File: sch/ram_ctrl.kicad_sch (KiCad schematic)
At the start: 11 parts

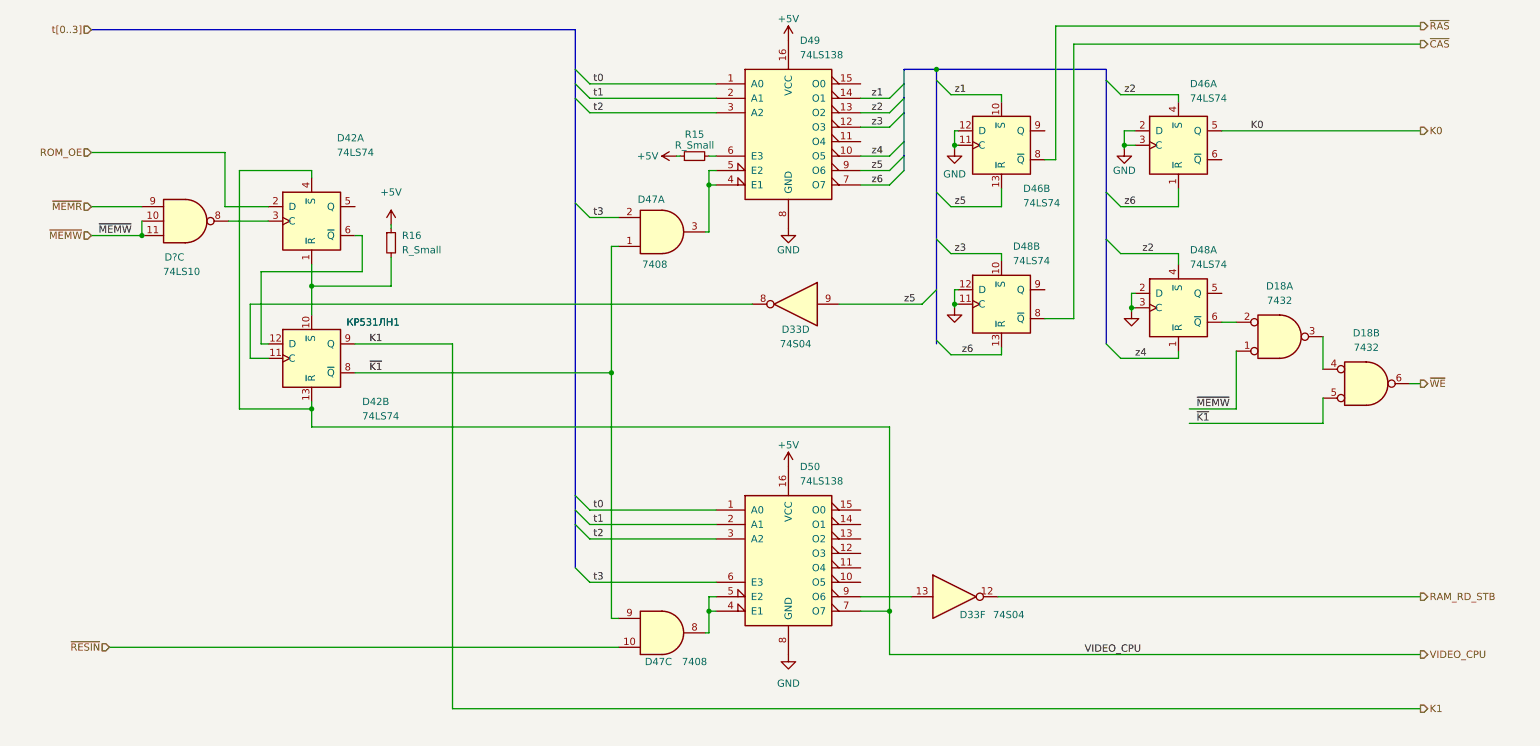
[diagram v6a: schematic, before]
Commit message: Schematics complete
Todo:
- part values
- full review
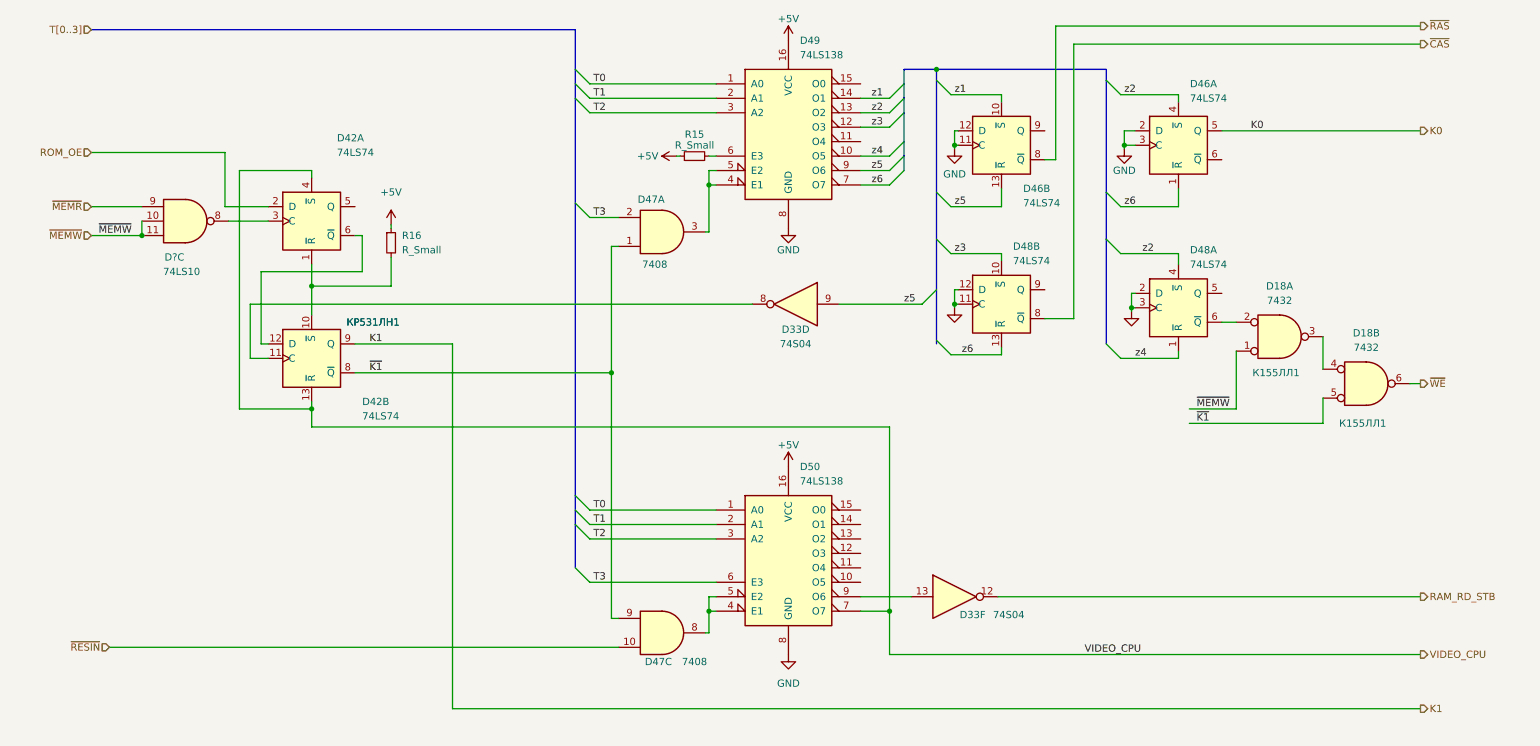
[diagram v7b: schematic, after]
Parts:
- D18: CCCP (none) -> К155ЛЛ1
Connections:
- net t0 renamed T0
- net t1 renamed T1
- net t2 renamed T2
- net t3 renamed T3
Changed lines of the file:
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@@
     (effects (font (size 1.27 1.27)) (justify left bottom))
   )
-  (label "t3" (at 119.38 124.46 0)
+  (label "T3" (at 119.38 124.46 0)
     (effects (font (size 1.27 1.27)) (justify left bottom))
   )
@@
     (effects (font (size 1.27 1.27)) (justify left bottom))
   )
-  (label "t0" (at 119.38 111.76 0)
+  (label "T0" (at 119.38 111.76 0)
     (effects (font (size 1.27 1.27)) (justify left bottom))
   )
@@
     (effects (font (size 1.27 1.27)) (justify left bottom))
   )
-  (label "t2" (at 119.38 116.84 0)
+  (label "T2" (at 119.38 116.84 0)
     (effects (font (size 1.27 1.27)) (justify left bottom))
   )
@@
     (effects (font (size 1.27 1.27)) (justify left bottom))
   )
-  (label "t1" (at 119.38 114.3 0)
+  (label "T1" (at 119.38 114.3 0)
     (effects (font (size 1.27 1.27)) (justify left bottom))
   )
@@
     (effects (font (size 1.27 1.27)) (justify left bottom))
   )
-  (label "t0" (at 119.38 36.83 0)
-    (effects (font (size 1.27 1.27)) (justify left bottom))
-  )
-  (label "t3" (at 119.38 60.325 0)
-    (effects (font (size 1.27 1.27)) (justify left bottom))
-  )
-  (label "t2" (at 119.38 41.91 0)
+  (label "T0" (at 119.38 36.83 0)
+    (effects (font (size 1.27 1.27)) (justify left bottom))
+  )
+  (label "T3" (at 119.38 60.325 0)
+    (effects (font (size 1.27 1.27)) (justify left bottom))
+  )
+  (label "T2" (at 119.38 41.91 0)
     (effects (font (size 1.27 1.27)) (justify left bottom))
   )
@@
     (effects (font (size 1.27 1.27)) (justify left bottom))
   )
-  (label "t1" (at 119.38 39.37 0)
+  (label "T1" (at 119.38 39.37 0)
     (effects (font (size 1.27 1.27)) (justify left bottom))
   )
@@
     (effects (font (size 1.27 1.27)) (justify right))
   )
-  (hierarchical_label "t[0..3]" (shape input) (at 31.115 27.305 180)
+  (hierarchical_label "T[0..3]" (shape input) (at 31.115 27.305 180)
     (effects (font (size 1.27 1.27)) (justify right))
   )
@@
   )
   (symbol (lib_id "74xx:74LS32") (at 255.27 89.535 0) (unit 2) (convert 2)
-    (in_bom yes) (on_board yes) (fields_autoplaced)
+    (in_bom yes) (on_board yes)
     (property "Reference" "D18" (id 0) (at 255.27 80.645 0))
     (property "Value" "7432" (id 1) (at 255.27 83.185 0))
@@
       (effects (font (size 1.27 1.27)) hide)
     )
+    (property "CCCP" "К155ЛЛ1" (id 4) (at 254.635 96.52 0))
     (pin "1")
     (pin "2")
@@
   )
   (symbol (lib_id "74xx:74LS32") (at 240.03 81.28 0) (mirror x) (unit 1) (convert 2)
-    (in_bom yes) (on_board yes) (fields_autoplaced)
+    (in_bom yes) (on_board yes)
     (property "Reference" "D18" (id 0) (at 240.03 72.39 0))
     (property "Value" "7432" (id 1) (at 240.03 74.93 0))
@@
       (effects (font (size 1.27 1.27)) hide)
     )
-    (pin "1")
-    (pin "2")
+    (property "CCCP" "К155ЛЛ1" (id 4) (at 239.395 87.63 0))
+    (pin "1")
+    (pin "2")

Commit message: Schematics completed with values
Visual corrections pending
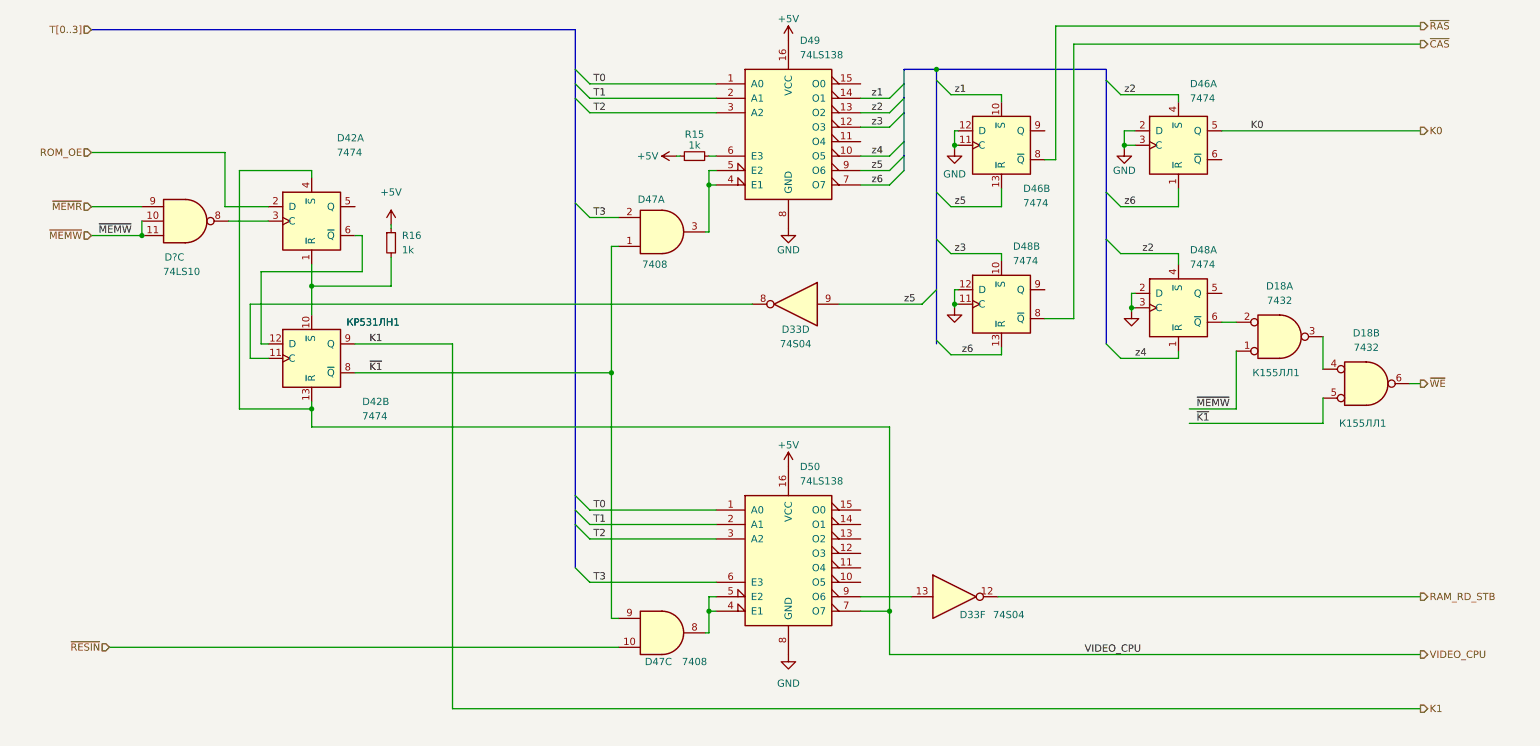
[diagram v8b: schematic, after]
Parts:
- D42, D46, D48: value 74LS74 -> 7474; CCCP (none) -> К155ТМ2
- D47: CCCP (none) -> К155ЛИ1
- D49, D50: CCCP (none) -> К155ИД7
- R15, R16: value R_Small -> 1k
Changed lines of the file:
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@@
       (effects (font (size 1.27 1.27)) (justify left))
     )
-    (property "Value" "74LS74" (id 1) (at 224.2694 39.37 0)
+    (property "Value" "7474" (id 1) (at 224.2694 39.37 0)
       (effects (font (size 1.27 1.27)) (justify left))
     )
@@
     )
     (property "Datasheet" "74xx/74hc_hct74.pdf" (id 3) (at 222.25 47.625 0)
+      (effects (font (size 1.27 1.27)) hide)
+    )
+    (property "CCCP" "К155ТМ2" (id 4) (at 222.25 47.625 0)
       (effects (font (size 1.27 1.27)) hide)
     )
@@
       (effects (font (size 1.27 1.27)) (justify left))
     )
-    (property "Value" "74LS74" (id 1) (at 78.74 95.25 0)
+    (property "Value" "7474" (id 1) (at 78.74 95.25 0)
       (effects (font (size 1.27 1.27)) (justify left))
     )
@@
     )
     (property "Datasheet" "74xx/74hc_hct74.pdf" (id 3) (at 69.85 85.09 0)
+      (effects (font (size 1.27 1.27)) hide)
+    )
+    (property "CCCP" "К155ТМ2" (id 4) (at 69.85 85.09 0)
       (effects (font (size 1.27 1.27)) hide)
     )
@@
       (effects (font (size 1.27 1.27)) hide)
     )
+    (property "CCCP" "К155ЛИ1" (id 4) (at 131.445 133.35 0)
+      (effects (font (size 1.27 1.27)) hide)
+    )
     (pin "1")
     (pin "2")
@@
       (effects (font (size 1.27 1.27)) (justify left))
     )
-    (property "Value" "74LS74" (id 1) (at 224.2694 68.58 0)
+    (property "Value" "7474" (id 1) (at 224.2694 68.58 0)
       (effects (font (size 1.27 1.27)) (justify left))
     )
@@
     )
     (property "Datasheet" "74xx/74hc_hct74.pdf" (id 3) (at 222.25 76.2 0)
+      (effects (font (size 1.27 1.27)) hide)
+    )
+    (property "CCCP" "К155ТМ2" (id 4) (at 222.25 76.2 0)
       (effects (font (size 1.27 1.27)) hide)
     )
@@
       (effects (font (size 1.27 1.27)) (justify left))
     )
-    (property "Value" "R_Small" (id 1) (at 85.725 66.0399 0)
+    (property "Value" "1k" (id 1) (at 85.725 66.0399 0)
       (effects (font (size 1.27 1.27)) (justify left))
     )
@@
       (effects (font (size 1.27 1.27)) hide)
     )
+    (property "CCCP" "К155ЛИ1" (id 4) (at 131.445 62.865 0)
+      (effects (font (size 1.27 1.27)) hide)
+    )
     (pin "1")
     (pin "2")
@@
       (effects (font (size 1.27 1.27)) (justify left))
     )
-    (property "Value" "74LS74" (id 1) (at 194.945 57.785 0)
+    (property "Value" "7474" (id 1) (at 194.945 57.785 0)
       (effects (font (size 1.27 1.27)) (justify left))
     )
@@
     )
     (property "Datasheet" "74xx/74hc_hct74.pdf" (id 3) (at 191.135 47.625 0)
+      (effects (font (size 1.27 1.27)) hide)
+    )
+    (property "CCCP" "К155ТМ2" (id 4) (at 191.135 47.625 0)
       (effects (font (size 1.27 1.27)) hide)
     )
@@
       (effects (font (size 1.27 1.27)) (justify left))
     )
-    (property "Value" "74LS74" (id 1) (at 74.295 48.895 0)
+    (property "Value" "7474" (id 1) (at 74.295 48.895 0)
       (effects (font (size 1.27 1.27)) (justify left))
     )
@@
     )
     (property "Datasheet" "74xx/74hc_hct74.pdf" (id 3) (at 69.85 60.96 0)
+      (effects (font (size 1.27 1.27)) hide)
+    )
+    (property "CCCP" "К155ТМ2" (id 4) (at 69.85 60.96 0)
       (effects (font (size 1.27 1.27)) hide)
     )
@@
       (effects (font (size 1.27 1.27)) (justify left))
     )
-    (property "Value" "74LS74" (id 1) (at 193.1544 67.945 0)
+    (property "Value" "7474" (id 1) (at 193.1544 67.945 0)
       (effects (font (size 1.27 1.27)) (justify left))
     )
@@
     )
     (property "Datasheet" "74xx/74hc_hct74.pdf" (id 3) (at 191.135 75.565 0)
+      (effects (font (size 1.27 1.27)) hide)
+    )
+    (property "CCCP" "К155ТМ2" (id 4) (at 191.135 75.565 0)
       (effects (font (size 1.27 1.27)) hide)
     )
@@
       (effects (font (size 1.27 1.27)) hide)
     )
+    (property "CCCP" "К155ИД7" (id 4) (at 153.67 119.38 0)
+      (effects (font (size 1.27 1.27)) hide)
+    )
     (pin "1")
     (pin "10")
@@
       (effects (font (size 1.27 1.27)) hide)
     )
+    (property "CCCP" "К155ИД7" (id 4) (at 153.67 44.45 0)
+      (effects (font (size 1.27 1.27)) hide)
+    )
     (pin "1")
     (pin "10")
@@
     (in_bom yes) (on_board yes)
     (property "Reference" "R15" (id 0) (at 137.16 45.72 90))
-    (property "Value" "R_Small" (id 1) (at 137.16 47.625 90))
+    (property "Value" "1k" (id 1) (at 137.16 47.625 90))
     (property "Footprint" "" (id 2) (at 137.16 49.53 0)
       (effects (font (size 1.27 1.27)) hide)
